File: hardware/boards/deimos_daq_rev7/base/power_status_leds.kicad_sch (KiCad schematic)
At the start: 5 parts

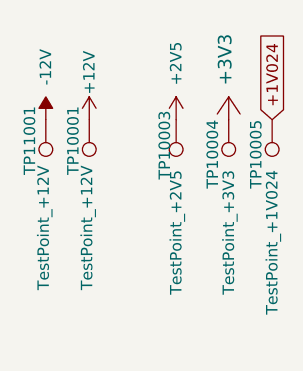
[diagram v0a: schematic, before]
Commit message: add more capacitance on 24V supply
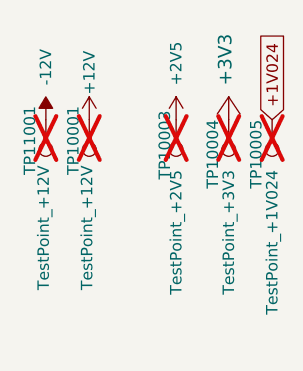
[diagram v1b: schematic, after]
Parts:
- TP10001, TP10003, TP10004, TP10005, TP11001: now not fitted
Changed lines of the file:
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@@
 		(exclude_from_sim no)
 		(in_bom no)
-		(on_board yes)
-		(dnp no)
+		(on_board no)
+		(dnp yes)
 		(property "Reference" "TP10003"
 			(at 183.642 81.026 90)
@@
 		(exclude_from_sim no)
 		(in_bom no)
-		(on_board yes)
-		(dnp no)
+		(on_board no)
+		(dnp yes)
 		(property "Reference" "TP10005"
 			(at 193.802 82.042 90)
@@
 		(exclude_from_sim no)
 		(in_bom no)
-		(on_board yes)
-		(dnp no)
+		(on_board no)
+		(dnp yes)
 		(property "Reference" "TP10001"
 			(at 173.482 80.518 90)
@@
 		(exclude_from_sim no)
 		(in_bom no)
-		(on_board yes)
-		(dnp no)
+		(on_board no)
+		(dnp yes)
 		(property "Reference" "TP11001"
 			(at 168.656 80.518 90)
@@
 		(exclude_from_sim no)
 		(in_bom no)
-		(on_board yes)
-		(dnp no)
+		(on_board no)
+		(dnp yes)
 		(property "Reference" "TP10004"
 			(at 188.976 82.042 90)
